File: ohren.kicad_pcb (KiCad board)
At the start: 2 copper layers, 60 x 28.7 mm, 36 parts, among them J1 Conn_01x19_MountingPin, U1 TLC5951RHA, U2 TLC5951RHA

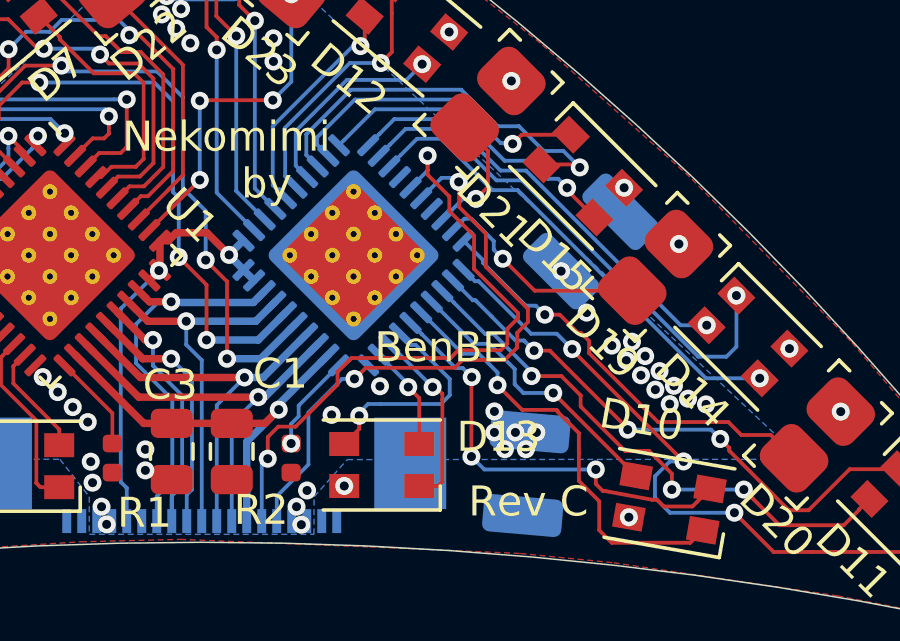
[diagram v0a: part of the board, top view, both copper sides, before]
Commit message: Reroute GSSOUT and DCSOUT to optimize cooling of U2
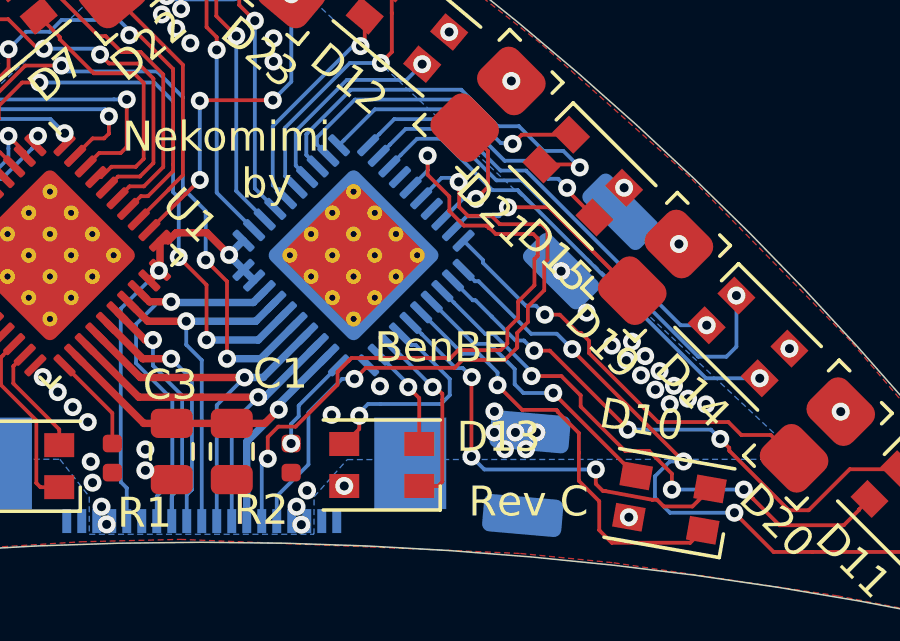
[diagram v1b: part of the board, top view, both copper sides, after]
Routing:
- net /DCSOUT: track 20.5 -> 22.3 mm
- net /GSSOUT: track 21.6 -> 23.3 mm

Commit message: Add additional via stitching to GND of U2
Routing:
- net GND: vias 52 -> 55
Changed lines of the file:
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@@
     (thickness 1.6)
     (drawings 18)
-    (tracks 795)
+    (tracks 798)
     (zones 0)
     (modules 36)
@@
   (gr_arc (start 83 177) (end 170 116) (angle -22.52944362) (layer Edge.Cuts) (width 0.05))
   (gr_arc (start 140 236) (end 170 116) (angle -28.07248694) (layer Edge.Cuts) (width 0.05))
-  (via (at 130.035 108.64) (size 0.6) (drill 0.3) (layers F.Cu B.Cu) (net 31))
-  (via (at 149.755 108.645) (size 0.6) (drill 0.3) (layers F.Cu B.Cu) (net 31))
   (segment (start 137.02 94.04) (end 138.896499 95.916499) (width 0.127) (layer F.Cu) (net 5))
   (segment (start 138.896499 100.551268) (end 137.90101 101.546757) (width 0.127) (layer F.Cu) (net 5))
@@
   (segment (start 141.5 111.4) (end 141.5 108.951651) (width 0.25) (layer B.Cu) (net 30))
   (segment (start 141.5 111.4) (end 141.5 111.765) (width 0.25) (layer B.Cu) (net 30))
+  (via (at 130.035 108.64) (size 0.6) (drill 0.3) (layers F.Cu B.Cu) (net 31))
+  (via (at 149.755 108.645) (size 0.6) (drill 0.3) (layers F.Cu B.Cu) (net 31))
   (via (at 132.14 106.54) (size 0.6) (drill 0.3) (layers F.Cu B.Cu) (net 31))
   (via (at 138.12 109.21) (size 0.6) (drill 0.3) (layers F.Cu B.Cu) (net 31))
@@
   (via (at 150.805 109.205) (size 0.6) (drill 0.3) (layers F.Cu B.Cu) (net 31))
   (via (at 143.51 110.58) (size 0.6) (drill 0.3) (layers F.Cu B.Cu) (net 31))
+  (via (at 150.52 102.64) (size 0.6) (drill 0.3) (layers F.Cu B.Cu) (net 31))
+  (via (at 150.52 103.28) (size 0.6) (drill 0.3) (layers F.Cu B.Cu) (net 31))
+  (via (at 149.88 102.64) (size 0.6) (drill 0.3) (layers F.Cu B.Cu) (net 31))
   (via (at 141.15 95.43) (size 0.6) (drill 0.3) (layers F.Cu B.Cu) (net 32))
   (segment (start 140.486499 94.766499) (end 141.15 95.43) (width 0.127) (layer F.Cu) (net 32))

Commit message: Add via stitching to low-impedance cap GNDs
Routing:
- net GND: vias 55 -> 58
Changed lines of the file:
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@@
     (thickness 1.6)
     (drawings 18)
-    (tracks 798)
+    (tracks 801)
     (zones 0)
     (modules 36)
@@
   (gr_arc (start 83 177) (end 170 116) (angle -22.52944362) (layer Edge.Cuts) (width 0.05))
   (gr_arc (start 140 236) (end 170 116) (angle -28.07248694) (layer Edge.Cuts) (width 0.05))
+  (via (at 138.995 93.48) (size 0.6) (drill 0.3) (layers F.Cu B.Cu) (net 31))
+  (via (at 139.485 93.885) (size 0.6) (drill 0.3) (layers F.Cu B.Cu) (net 31))
+  (via (at 152.63 103.63) (size 0.6) (drill 0.3) (layers F.Cu B.Cu) (net 31))
   (segment (start 137.02 94.04) (end 138.896499 95.916499) (width 0.127) (layer F.Cu) (net 5))
   (segment (start 138.896499 100.551268) (end 137.90101 101.546757) (width 0.127) (layer F.Cu) (net 5))

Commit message: Design revision D
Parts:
- removed C1: C, Capacitor_SMD:C_0805_2012Metric
- removed R1, R2: 2k4, Resistor_SMD:R_0402_1005Metric
- removed REF** (x3): MountingHole_1.5mm, catear-pcb:MountingHole_1mm
- removed U2: TLC5951RHA, Package_DFN_QFN:Texas_S-PVQFN-N40_EP4.15x4.15mm_ThermalVias
- C2, C5, C6, C7, C8: footprint Capacitor_SMD:C_1210_3225Metric -> Capacitor_SMD:C_0805_2012Metric; moved to F.Cu
- U1: value TLC5951RHA -> TLC5955RTQ; footprint Package_DFN_QFN:Texas_S-PVQFN-N40_EP4.15x4.15mm_ThermalVias -> Package_DFN_QFN:QFN-56-1EP_8x8mm_P0.5mm_EP5.6x5.6mm_ThermalVias
- moved C5 7.74 mm to (130.0, 103.1), turned to 0 degrees
- moved U1 5.11 mm to (140.0, 102.0), turned to 270 degrees
- moved C8 3.04 mm to (150.0, 103.1), turned to 180 degrees
- moved C2 2.65 mm to (140.0, 94.9)
- moved C3 0.78 mm to (138.8, 108.5), turned to 0 degrees
- moved J1 0.46 mm to (140.0, 111.1)
- moved D25 0.17 mm to (119.5, 108.7)
- moved D8 0.09 mm to (116.4, 111.2), turned to 225 degrees
- turned C6 to 80 degrees
- turned C7 to 100 degrees
- turned D3 to 0 degrees
- turned D4 to 225 degrees
- turned D5 to 225 degrees
- turned D6 to 180 degrees
- turned D7 to 220 degrees
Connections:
- D10 pad 1: /U2_R6 -> /U1_R0
- D10 pad 2: /U2_G6 -> /U1_G0
- D10 pad 3: /U2_B6 -> /U1_B0
- D11 pad 1: /U2_R5 -> /U1_R5
- D11 pad 2: /U2_G5 -> /U1_G5
- D11 pad 3: /U2_B5 -> /U1_B5
- D12 pad 1: /U2_R1 -> /U1_R3
- D12 pad 2: /U2_G1 -> /U1_G3
- D12 pad 3: /U2_B1 -> /U1_B3
- D13 pad 1: /U2_R7 -> /U1_R4
- D13 pad 2: /U2_G7 -> /U1_G4
- D13 pad 3: /U2_B7 -> /U1_B4
- D14 pad 1: /U2_R3 -> /U1_R1
- D14 pad 2: /U2_G3 -> /U1_G1
- D14 pad 3: /U2_B3 -> /U1_B1
- D15 pad 1: /U2_R2 -> /U1_R6
- D15 pad 2: /U2_G2 -> /U1_G6
- D15 pad 3: /U2_B2 -> /U1_B6
- D19 pad 1: /U2_R4 -> /U1_R2
- D20 pad 1: /U2_G4 -> /U1_B2
- D21 pad 1: /U2_B4 -> /U1_G2
- D22 pad 1: /U1_R0 -> /U1_G7
- D23 pad 1: /U1_G0 -> /U1_R7
- D24 pad 1: /U1_B0 -> /U1_G14
- D25 pad 1: /U1_G4 -> /U1_B14
- D26 pad 1: /U1_R4 -> /U1_R14
- D3 pad 1: /U1_R7 -> /U1_R8
- D3 pad 2: /U1_G7 -> /U1_G8
- D3 pad 3: /U1_B7 -> /U1_B8
- D4 pad 1: /U1_R2 -> /U1_R10
- D4 pad 2: /U1_G2 -> /U1_G10
- D4 pad 3: /U1_B2 -> /U1_B10
- D5 pad 1: /U1_R3 -> /U1_R13
- D5 pad 2: /U1_G3 -> /U1_G13
- D5 pad 3: /U1_B3 -> /U1_B13
- D6 pad 1: /U2_R0 -> /U1_R11
- D6 pad 2: /U2_G0 -> /U1_G11
- D6 pad 3: /U2_B0 -> /U1_B11
- D7 pad 1: /U1_R1 -> /U1_R15
- D7 pad 2: /U1_G1 -> /U1_G15
- D7 pad 3: /U1_B1 -> /U1_B15
- D8 pad 1: /U1_R5 -> /U1_R9
- D8 pad 2: /U1_G5 -> /U1_G9
- D8 pad 3: /U1_B5 -> /U1_B9
- D9 pad 1: /U1_R6 -> /U1_R12
- D9 pad 2: /U1_G6 -> /U1_G12
- D9 pad 3: /U1_B6 -> /U1_B12
- J1 pad 10: /GSSCK -> /SCLK
- J1 pad 11: /DCSCK -> GND
- J1 pad 12: /XBLNK -> /LAT
- J1 pad 13: VDD -> GND
- J1 pad 14: /GSSOUT -> /SOUT
- J1 pad 15: /DCSOUT -> GND
- J1 pad 4: GND -> VDD
- J1 pad 5: /GSCKB -> GND
- J1 pad 6: GND -> /GSCLK
- J1 pad 7: /GSLAT -> GND
- J1 pad 8: /GSSIN -> /SIN
- J1 pad 9: /DCSIN -> GND
- J1 pad MP: VCC -> GND
- U1 pad 1: /U1_G3 -> /U1_B3
- U1 pad 10: /U1_G4 -> /U1_R11
- U1 pad 11: /U1_B5 -> /U1_B11
- U1 pad 12: /U1_R5 -> /U1_G15
- U1 pad 13: /U1_G5 -> /U1_R15
- U1 pad 14: /U1_B6 -> /U1_B15
- U1 pad 15: /U1_R6 -> /U1_G10
- U1 pad 16: /U1_G6 -> /U1_R10
- U1 pad 17: /U1_B7 -> /U1_B10
- U1 pad 18: /U1_R7 -> /U1_G14
- U1 pad 19: /U1_G7 -> /U1_R14
- U1 pad 20: GND -> /U1_B14
- U1 pad 21: Net-(R1-Pad1) -> /U1_G13
- U1 pad 22: VDD -> /U1_R13
- U1 pad 23: /XBLNK -> /U1_B13
- U1 pad 24: /DCSCK -> /U1_G9
- U1 pad 25: /DCSIN -> /U1_R9
- U1 pad 26: /GSSIN -> /U1_B9
- U1 pad 27: /GSSCK -> /U1_G12
- U1 pad 28: /GSLAT -> /U1_R12
- U1 pad 29: /GSCKB -> /U1_B12
- U1 pad 3: /U1_B3 -> /U1_G3
- U1 pad 30: /GSCKB -> /U1_G8
- U1 pad 31: /GSCKB -> /U1_R8
- U1 pad 32: /U1_G0 -> /U1_B8
- U1 pad 33: /U1_R0 -> VDD
- U1 pad 34: /U1_B0 -> /GSCLK
- U1 pad 35: /U1_G1 -> GND
- U1 pad 36: /U1_R1 -> /SIN
- U1 pad 37: /U1_B1 -> /SCLK
- U1 pad 38: /U1_G2 -> /LAT
- U1 pad 39: /U1_R2 -> /U1_B4
- U1 pad 4: Net-(U1-Pad4) -> /U1_B7
- U1 pad 40: /U1_B2 -> /U1_R4
- U1 pad 41: GND -> /U1_G4
- U1 pad 5: /GSSCHAIN -> /U1_R7
- U1 pad 6: /DCSCHAIN -> /U1_G7
- U1 pad 7: Net-(U1-Pad7) -> /SOUT
- U1 pad 8: /U1_B4 -> GND
- U1 pad 9: /U1_R4 -> /U1_G11
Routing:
- net /SOUT: track 0.00 -> 27.9 mm, vias 0 -> 1
- net /U1_B9: track 0.00 -> 25.8 mm
- net /U1_G9: track 0.00 -> 23.4 mm
- net /DCSCHAIN: track 23.4 -> 0.00 mm, vias 3 -> 0
- net /GSSOUT: track 23.3 -> 0.00 mm, vias 2 -> 0
- net /U1_G13: track 0.00 -> 23.2 mm
- net /U1_R13: track 0.00 -> 22.6 mm
- net /U1_R9: track 0.00 -> 22.5 mm
- net /DCSOUT: track 22.3 -> 0.00 mm, vias 2 -> 0
- net /U2_B5: track 21.5 -> 0.00 mm, vias 3 -> 0
- net /GSSCHAIN: track 21.2 -> 0.00 mm, vias 3 -> 0
- net VCC: track 0.85 -> 22.0 mm, vias 21 -> 26
- net /U1_B13: track 0.00 -> 20.9 mm
- net /U1_B14: track 0.00 -> 19.9 mm, vias 0 -> 2
- net /U2_R5: track 18.7 -> 0.00 mm, vias 3 -> 0
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
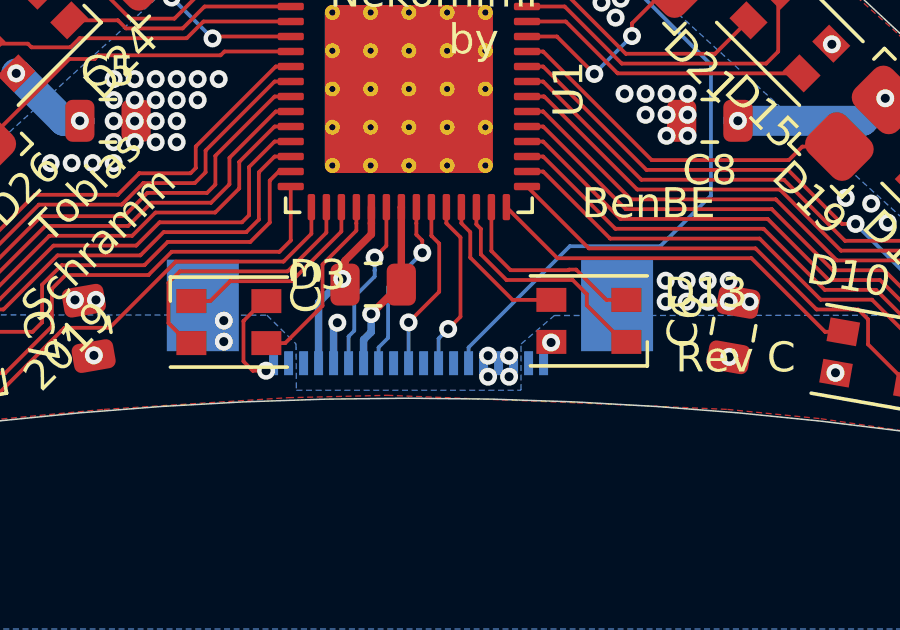
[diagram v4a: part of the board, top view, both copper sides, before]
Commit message: Revise connector layout
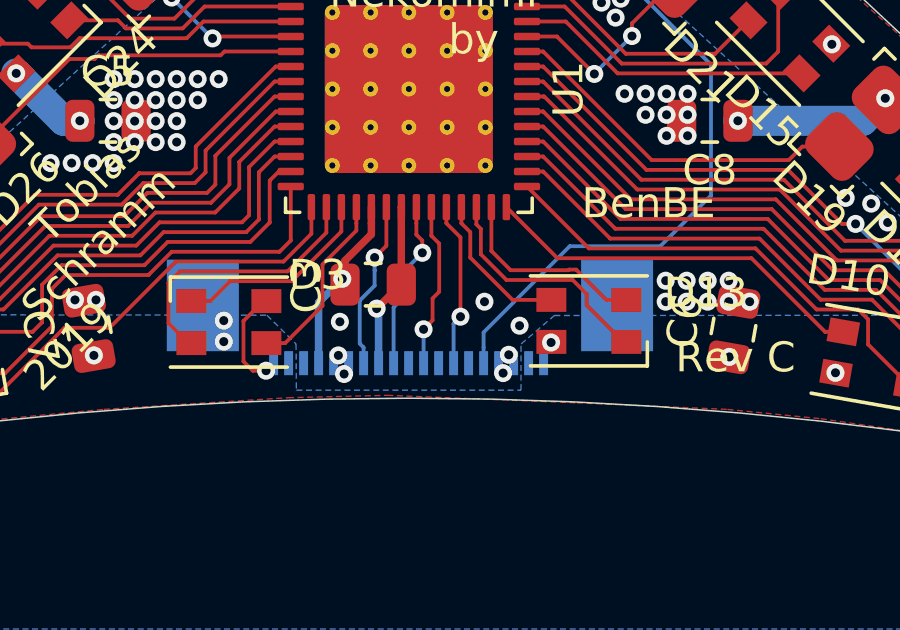
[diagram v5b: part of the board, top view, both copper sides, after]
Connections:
- J1 pad 10: /SCLK -> GND
- J1 pad 11: GND -> /SCLK
- J1 pad 12: /LAT -> GND
- J1 pad 13: GND -> /LAT
- J1 pad 14: /SOUT -> GND
- J1 pad 15: GND -> /SOUT
- J1 pad 6: /GSCLK -> GND
- J1 pad 7: GND -> /GSCLK
- J1 pad 8: /SIN -> GND
- J1 pad 9: GND -> /SIN
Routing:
- net GND: track 7.14 -> 5.61 mm, vias 73 -> 75
